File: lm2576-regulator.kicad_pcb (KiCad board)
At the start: 2 copper layers, 58.4 x 30.5 mm, 9 parts, among them J1 Barrel Jack, J2 KLS2, U1 LM2576HVS-5

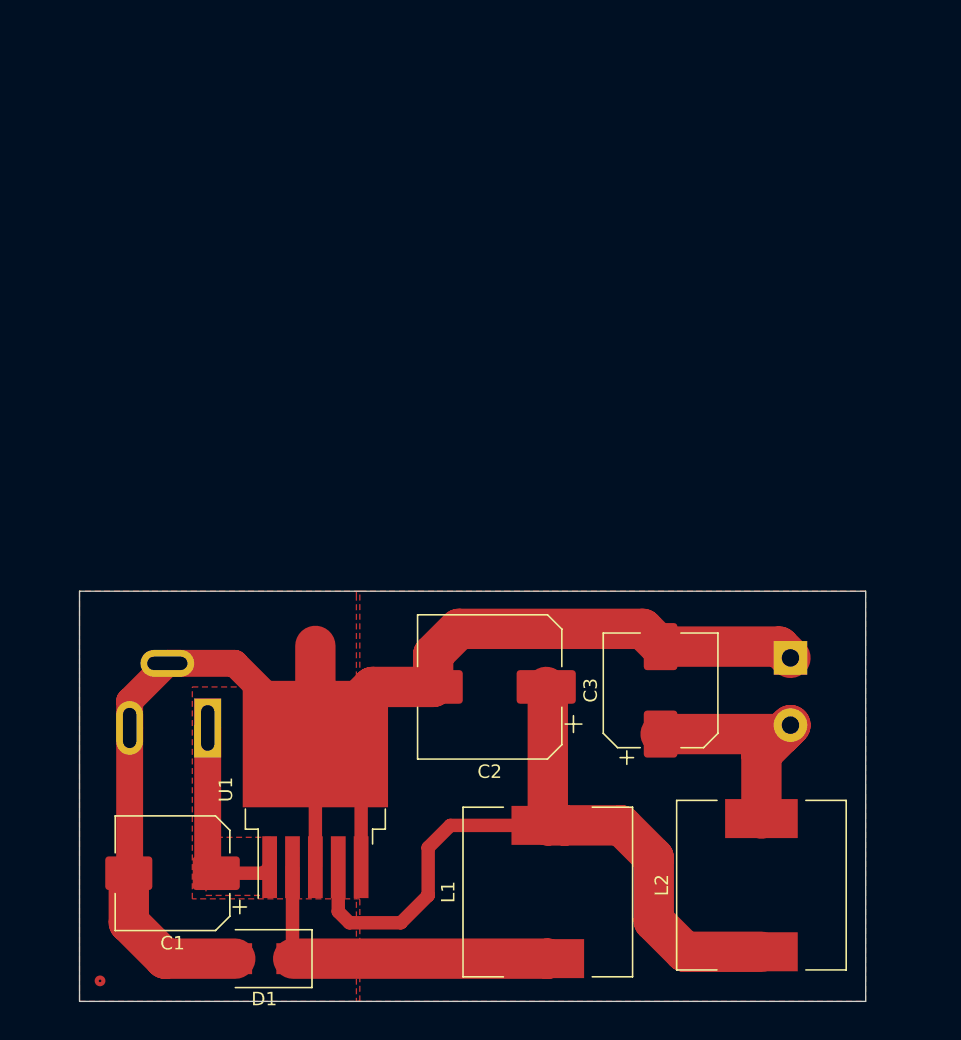
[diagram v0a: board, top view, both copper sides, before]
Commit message: Made improvements for production on a factory
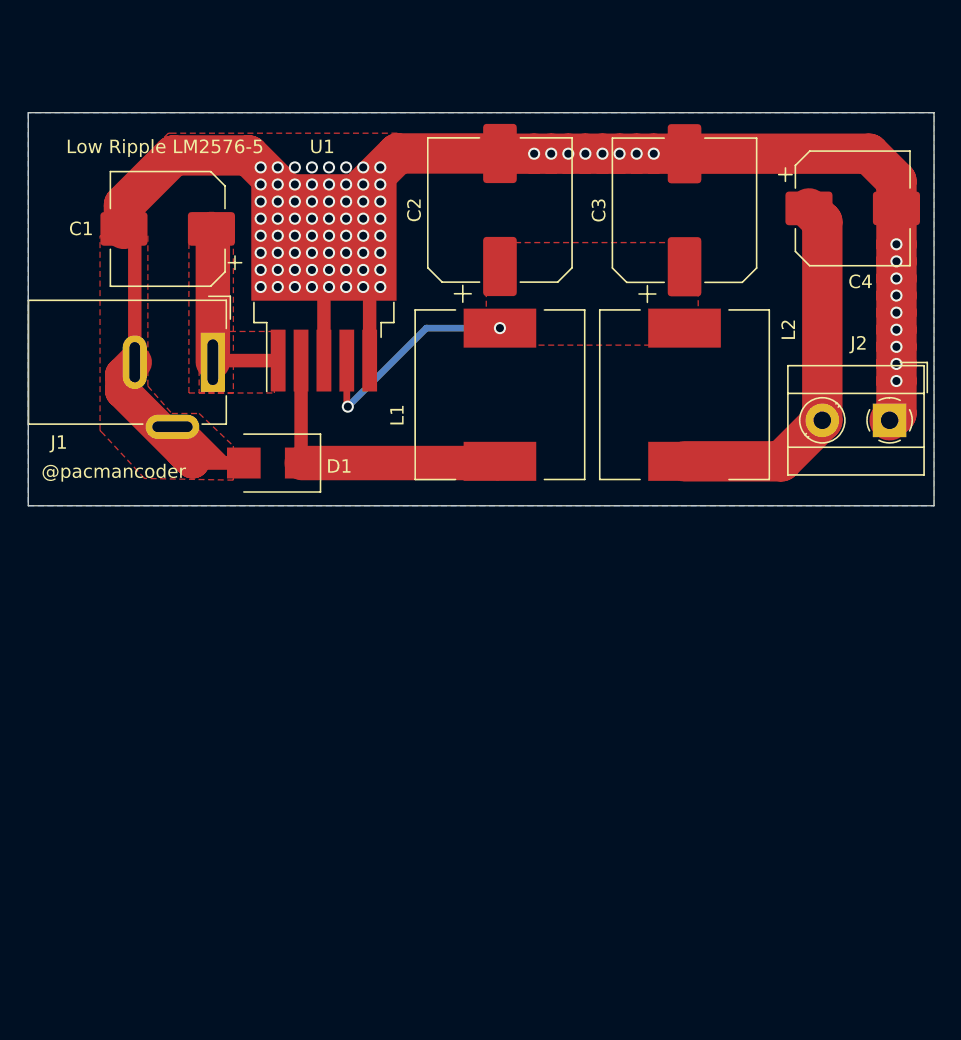
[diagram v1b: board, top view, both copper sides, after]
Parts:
- added C4: 100uF, Capacitor_SMD:CP_Elec_8x10, F.Cu at (212.4, 51.6)
- C3: value 100uF -> 1000uF; footprint Capacitor_SMD:CP_Elec_8x10 -> Capacitor_SMD:CP_Elec_10x10.5
- J1, J2: moved to F.Cu
- L2: value 20uH -> 22uH
- moved C1 47.9 mm to (161.5, 53.1)
- moved U1 37.7 mm to (173.1, 57.1)
- moved L1 37.1 mm to (186.2, 65.4)
- moved L2 36.9 mm to (199.9, 65.4), turned to 270 degrees
- moved D1 36.8 mm to (169.3, 70.5)
- moved C3 35.7 mm to (199.9, 51.7)
- moved C2 35.5 mm to (186.2, 51.7), turned to 90 degrees
- moved J1 27.2 mm to (164.8, 63.0), turned to 270 degrees
- moved J2 19.1 mm to (215.1, 67.3), turned to 180 degrees
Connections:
- net Net-(D1-Pad1) renamed /SCHOTTKY
- C3 pad 1: VOUT -> FILTER_IN
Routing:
- net FILTER_IN: track 58.7 -> 17.2 mm, vias 0 -> 2
- net GND: track 106.3 -> 135.5 mm, vias 0 -> 77
- net VOUT: track 17.8 -> 27.7 mm
- net /SCHOTTKY: track 30.9 -> 22.3 mm
- net VIN: track 17.1 -> 14.9 mm
- net (no net): vias 0 -> 4
- added copper zone on F.Cu, net FILTER_IN
- added copper zone on B.Cu, net GND
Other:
- board size 58.4 x 30.5 mm -> 67.3 x 29.2 mm
- net class Default: clearance 0.2 -> 0.25; via_dia 0.8 -> 0.9; via_drill 0.4 -> 0.6
- rule trace_clearance: 0.2 -> 0.25
- rule trace_min: 0.2 -> 0.25
- rule via_min_drill: 0.3 -> 0.6
- rule via_min_size: 0.4 -> 0.9
- board text added: "@pacmancoder"
- board text added: "Low Ripple LM2576-5"

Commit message: Modified after review of Alexander
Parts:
- D1: footprint Diode_SMD:D_SMB -> Diode_SMD:D_SMC
- moved C1 7.51 mm to (160.0, 45.7), turned to 90 degrees
- moved C3 5.22 mm to (199.9, 46.5)
- moved C2 5.20 mm to (186.2, 46.5)
- moved C4 3.06 mm to (212.1, 54.6)
- moved J1 3.05 mm to (164.8, 59.9)
- moved D1 1.18 mm to (169.6, 69.3)
- moved J2 0.36 mm to (214.9, 67.6)
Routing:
- net GND: track 135.5 -> 126.1 mm, vias 77 -> 79
- net FILTER_IN: track 17.2 -> 24.7 mm
- net VOUT: track 27.7 -> 24.5 mm
- net /SCHOTTKY: track 22.3 -> 20.5 mm
- net (no net): vias 4 -> 0
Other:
- board size 67.3 x 29.2 mm -> 67.3 x 35.6 mm
- net class Default: via_dia 0.9 -> 1.1
- rule via_min_size: 0.9 -> 1.1
